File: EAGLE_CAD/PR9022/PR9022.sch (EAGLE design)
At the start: 72 parts, among them SW1 C&K_PTS645, U1 SI4702-C19-GMR, X1 ABS25XTAL

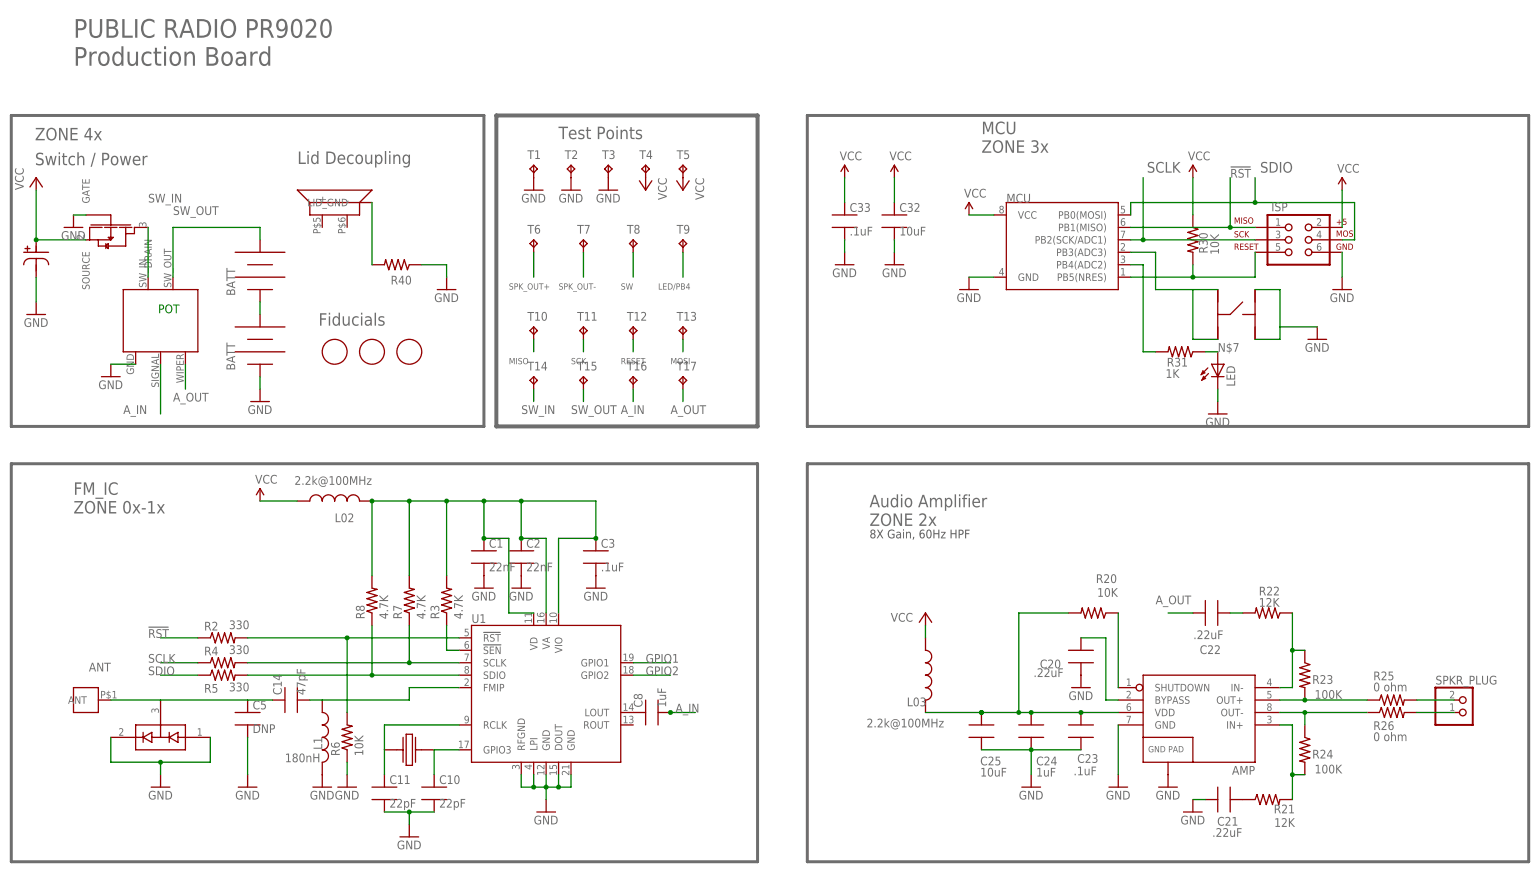
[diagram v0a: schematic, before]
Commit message: Updated PR9022 Layout
Rotated AMP circuitry 90deg
Added spacing on C23, C24, C25, C21, R21
Added updated speaker footprint w/M3 PemNuts
Added updated antenna footprint w/M3 PemNuts
Rerouted MCU traced to accommodate new SPK placement
Rerouted power, and audio traces to accommodate new SPK placement
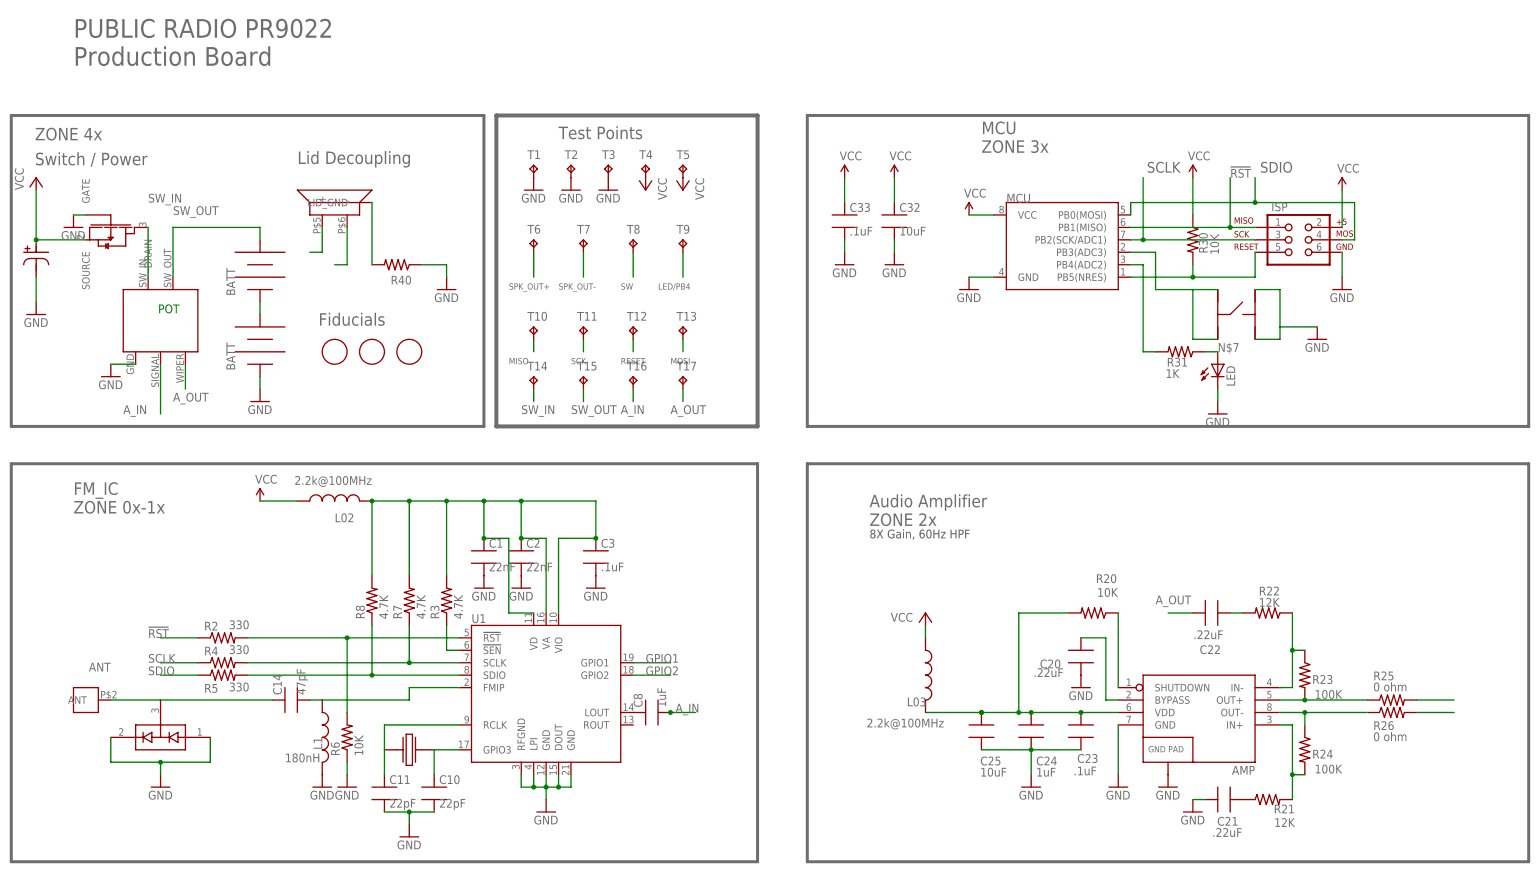
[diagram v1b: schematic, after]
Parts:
- removed C5: DNP, PR_Parts_Library:C_SMT_0603_CPL
- removed SPKR_PLUG: (no value), PR_Parts_Library:JST_2PIN-SMT-RA
- ANT_MOUNT: device PR_Parts_Library:M3_SCREW_POST -> PR_Parts_Library:M3_PEMNUT
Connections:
- net ANT: no longer C5.1
- net GND: no longer C5.2
- net SPK_OUT+: now also SPKR_PLACE.-; no longer SPKR_PLUG.1
- net SPK_OUT-: now also SPKR_PLACE.+; no longer SPKR_PLUG.2
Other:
- note added: "PUBLIC RADIO PR9022 Production Board"
- note removed: "PUBLIC RADIO PR9020 Production Board"
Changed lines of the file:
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@@
 <?xml version="1.0" encoding="utf-8"?>
 <!DOCTYPE eagle SYSTEM "eagle.dtd">
-<eagle version="6.6.0">
+<eagle version="7.2.0">
 <drawing>
 <settings>
@@
 <part name="GND24" library="SparkFun-Aesthetics" deviceset="GND" device=""/>
 <part name="P+1" library="supply1" deviceset="VCC" device=""/>
-<part name="ANT_MOUNT" library="PR_Parts_Library" deviceset="M3_SCREW_POST" device="" value="DNP"/>
+<part name="ANT_MOUNT" library="PR_Parts_Library" deviceset="M3_PEMNUT" device="" value="DNP"/>
 <part name="R1" library="PR_Parts_Library" deviceset="RV170SF_TAIWANA_POT_SW" device="" value="">
 <attribute name="MFG_PN" value="RV170SF-43-20F-A10K - supplied by CL Labs"/>
@@
 <attribute name="TOL" value="1%"/>
 </part>
-<part name="GND6" library="SparkFun-Aesthetics" deviceset="GND" device=""/>
 <part name="L1" library="PR_Parts_Library" deviceset="L_SMT" device="_0805_ADAFRUIT" value="180nH">
 <attribute name="CURRENT" value="400mA"/>
@@
 </part>
 <part name="SUPPLY1" library="SparkFun-Aesthetics" deviceset="VCC" device=""/>
-<part name="SPKR_PLUG" library="PR_Parts_Library" deviceset="JST_2PIN" device="-SMT-RA"/>
-<part name="C5" library="PR_Parts_Library" deviceset="C_SMT" device="_0603_CPL" value="DNP">
-<attribute name="MFG_PN" value="DNP"/>
-<attribute name="TOL" value="2%"/>
-<attribute name="VOLTAGE" value="50V"/>
-</part>
 <part name="C14" library="PR_Parts_Library" deviceset="C_SMT" device="_0603_CPL" value="47pF">
 <attribute name="MFG_PN" value="CL10C470JB8NCNC"/>
@@
 <text x="157.48" y="144.78" size="2.54" layer="96">MCU
 ZONE 3x</text>
-<text x="-27.94" y="162.56" size="3.81" layer="96">PUBLIC RADIO PR9020
+<text x="-27.94" y="162.56" size="3.81" layer="96">PUBLIC RADIO PR9022
 Production Board </text>
 <text x="22.098" y="109.474" size="2.54" layer="96">Fiducials </text>
@@
 <instance part="GND20" gate="1" x="63.5" y="55.88"/>
 <instance part="GND9" gate="1" x="27.94" y="15.24"/>
-<instance part="SUPPLY5" gate="G$1" x="10.16" y="73.66"/>
+<instance part="SUPPLY5" gate="1" x="10.16" y="73.66"/>
 <instance part="R21" gate="G$1" x="215.9" y="12.7" smashed="yes">
 <attribute name="NAME" x="221.488" y="11.6586" size="1.778" layer="95" rot="R180"/>
@@
 <instance part="GND3" gate="1" x="-27.94" y="129.54"/>
 <instance part="MCU" gate="G$1" x="175.26" y="124.46"/>
-<instance part="SUPPLY8" gate="G$1" x="154.94" y="132.08"/>
+<instance part="SUPPLY8" gate="1" x="154.94" y="132.08"/>
 <instance part="GND25" gate="1" x="154.94" y="116.84"/>
 <instance part="GND23" gate="1" x="139.7" y="121.92"/>
 <instance part="GND22" gate="1" x="129.54" y="121.92"/>
-<instance part="SUPPLY6" gate="G$1" x="129.54" y="139.7"/>
-<instance part="SUPPLY7" gate="G$1" x="139.7" y="139.7"/>
+<instance part="SUPPLY6" gate="1" x="129.54" y="139.7"/>
+<instance part="SUPPLY7" gate="1" x="139.7" y="139.7"/>
 <instance part="GND31" gate="1" x="226.06" y="106.68"/>
 <instance part="ISP" gate="G$1" x="220.98" y="127"/>
 <instance part="GND30" gate="1" x="205.74" y="91.44"/>
-<instance part="SUPPLY9" gate="G$1" x="231.14" y="137.16"/>
+<instance part="SUPPLY9" gate="1" x="231.14" y="137.16"/>
 <instance part="GND32" gate="1" x="231.14" y="116.84"/>
 <instance part="R31" gate="G$1" x="198.12" y="104.14" smashed="yes" rot="R180">
@@
 <attribute name="VALUE" x="195.072" y="98.806" size="1.778" layer="96"/>
 </instance>
-<instance part="GND6" gate="1" x="7.62" y="15.24"/>
 <instance part="L1" gate="G$1" x="22.86" y="25.4" smashed="yes">
 <attribute name="NAME" x="22.86" y="22.86" size="1.778" layer="95" rot="R90"/>
@@
 <attribute name="VALUE" x="205.994" y="123.952" size="1.778" layer="96" rot="R90"/>
 </instance>
-<instance part="SUPPLY1" gate="G$1" x="200.66" y="139.7"/>
-<instance part="SPKR_PLUG" gate="G$1" x="256.54" y="30.48"/>
-<instance part="C5" gate="G$1" x="7.62" y="30.48"/>
+<instance part="SUPPLY1" gate="1" x="200.66" y="139.7"/>
 <instance part="C14" gate="G$1" x="15.24" y="33.02" rot="R90"/>
 <instance part="C11" gate="G$1" x="35.56" y="15.24"/>
@@
 <pinref part="GND7" gate="1" pin="GND"/>
 <pinref part="L1" gate="G$1" pin="2"/>
-</segment>
-<segment>
-<pinref part="GND6" gate="1" pin="GND"/>
-<wire x1="7.62" y1="25.4" x2="7.62" y2="17.78" width="0.1524" layer="91"/>
-<pinref part="C5" gate="G$1" pin="2"/>
 </segment>
 <segment>
@@
 <segment>
 <pinref part="MCU" gate="G$1" pin="VCC"/>
-<pinref part="SUPPLY8" gate="G$1" pin="VCC"/>
+<pinref part="SUPPLY8" gate="1" pin="VCC"/>
 <wire x1="160.02" y1="132.08" x2="154.94" y2="132.08" width="0.1524" layer="91"/>
 </segment>
 <segment>
 <pinref part="L02" gate="G$1" pin="1"/>
-<pinref part="SUPPLY5" gate="G$1" pin="VCC"/>
+<pinref part="SUPPLY5" gate="1" pin="VCC"/>
 <wire x1="17.78" y1="73.66" x2="10.16" y2="73.66" width="0.1524" layer="91"/>
 </segment>
@@
 <pinref part="ISP" gate="G$1" pin="2"/>
 <wire x1="231.14" y1="137.16" x2="231.14" y2="129.54" width="0.1524" layer="91"/>
-<pinref part="SUPPLY9" gate="G$1" pin="VCC"/>
-</segment>
-<segment>
-<pinref part="SUPPLY6" gate="G$1" pin="VCC"/>
+<pinref part="SUPPLY9" gate="1" pin="VCC"/>
+</segment>
+<segment>
+<pinref part="SUPPLY6" gate="1" pin="VCC"/>
 <pinref part="C33" gate="G$1" pin="1"/>
 <wire x1="129.54" y1="139.7" x2="129.54" y2="134.62" width="0.1524" layer="91"/>
 </segment>
 <segment>
-<pinref part="SUPPLY7" gate="G$1" pin="VCC"/>
+<pinref part="SUPPLY7" gate="1" pin="VCC"/>
 <wire x1="139.7" y1="139.7" x2="139.7" y2="134.62" width="0.1524" layer="91"/>
 <pinref part="C32" gate="G$1" pin="1"/>
@@
 <pinref part="R30" gate="G$1" pin="1"/>
 <wire x1="200.66" y1="132.08" x2="200.66" y2="139.7" width="0.1524" layer="91"/>
-<pinref part="SUPPLY1" gate="G$1" pin="VCC"/>
+<pinref part="SUPPLY1" gate="1" pin="VCC"/>
 </segment>
 <segment>
@@
 <wire x1="-20.32" y1="33.02" x2="-10.16" y2="33.02" width="0.1524" layer="91"/>
 <pinref part="C14" gate="G$1" pin="1"/>
-<pinref part="C5" gate="G$1" pin="1"/>
-<wire x1="7.62" y1="33.02" x2="12.7" y2="33.02" width="0.1524" layer="91"/>
-<wire x1="-10.16" y1="33.02" x2="7.62" y2="33.02" width="0.1524" layer="91"/>
+<wire x1="-10.16" y1="33.02" x2="12.7" y2="33.02" width="0.1524" layer="91"/>
 <label x="-20.32" y="40.64" size="1.778" layer="95" rot="R180"/>
 </segment>
@@
 </segment>
 <segment>
-<pinref part="SPKR_PLUG" gate="G$1" pin="1"/>
 <wire x1="246.38" y1="33.02" x2="254" y2="33.02" width="0.1524" layer="91"/>
 <pinref part="R25" gate="G$1" pin="2"/>
+</segment>
+<segment>
+<pinref part="SPKR_PLACE" gate="G$1" pin="-"/>
+<wire x1="27.94" y1="129.54" x2="27.94" y2="121.92" width="0.1524" layer="91"/>
+<wire x1="27.94" y1="121.92" x2="25.4" y2="121.92" width="0.1524" layer="91"/>
 </segment>
 </net>
@@
 </segment>
 <segment>
-<pinref part="SPKR_PLUG" gate="G$1" pin="2"/>
 <wire x1="246.38" y1="30.48" x2="254" y2="30.48" width="0.1524" layer="91"/>
 <pinref part="R26" gate="G$1" pin="2"/>
 </segment>
-</net>
+<segment>
+<pinref part="SPKR_PLACE" gate="G$1" pin="+"/>
+<wire x1="22.86" y1="129.54" x2="22.86" y2="124.46" width="0.1524" layer="91"/>
+<wire x1="22.86" y1="124.46" x2="20.32" y2="124.46" width="0.1524" layer="91"/>
+</segment>
+</net>
